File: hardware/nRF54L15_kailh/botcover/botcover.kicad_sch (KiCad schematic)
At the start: 143 parts

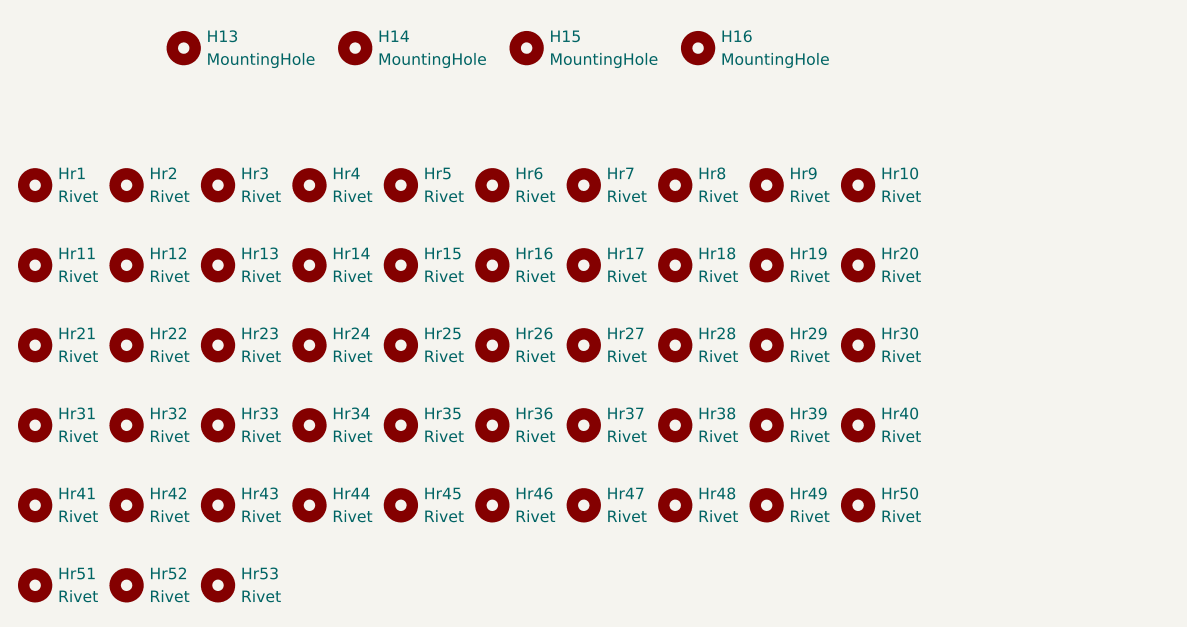
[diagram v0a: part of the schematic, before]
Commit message: M  hardware/nRF54L15_kailh/border.py M  hardware/nRF54L15_kailh/botcover/botcover.kicad_pcb M  hardware/nRF54L15_kailh/botcover/botcover.kicad_sch M  hardware/nRF54L15_kailh/pcb/pcb.kicad_pcb M  hardware/nRF54L15_kailh/pcb/pcb.kicad_sch M  hardware/nRF54L15_kailh/placefp.py A  hardware/nRF54L15_kailh/tmr-footprints/MountingHole_1.5mm_M1.4_NoPad.kicad_mod R  hardware/nRF54L15_kailh/tmr-footprints/SMTSO_M1.6.kicad_mod -> hardware/nRF54L15_kailh/tmr-footprints/SMTSO_M1.4_M1.6.kicad_mod
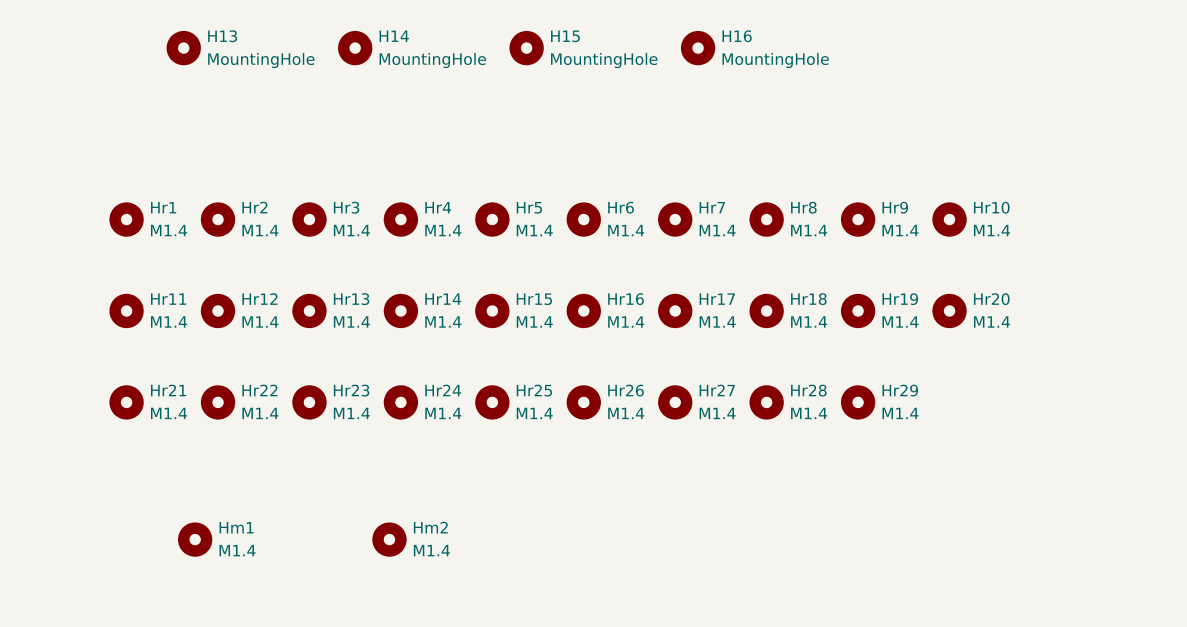
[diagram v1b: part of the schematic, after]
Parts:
- removed Hr30, Hr31, Hr32, Hr33, Hr34, Hr35, Hr36, Hr37, Hr38, Hr39, Hr40, Hr41, Hr42, Hr43, Hr44, Hr45, Hr46, Hr47, Hr48, Hr49, Hr50, Hr51, Hr52, Hr53: Rivet, tmr-lib:RivetClearanceHole_1.5mm, symbol Mechanical:MountingHole
- added Hm1, Hm2: M1.4, tmr-lib:MountingHole_1.5mm_M1.4_NoPad, symbol Mechanical:MountingHole
- Hr1, Hr10, Hr11, Hr12, Hr13, Hr14, Hr15, Hr16, Hr17, Hr18, Hr19, Hr2, Hr20, Hr21, Hr22, Hr23, Hr24, Hr25, Hr26, Hr27, Hr28, Hr29, Hr3, Hr4, Hr5, Hr6, Hr7, Hr8, Hr9: value Rivet -> M1.4; footprint tmr-lib:RivetClearanceHole_1.5mm -> tmr-lib:MountingHole_1.5mm_M1.4_NoPad
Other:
- moved on the sheet: Hr1

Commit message: M  .gitignore A  hardware/nRF54L15_gateron_kailh_TMR2615/LED.kicad_sch A  hardware/nRF54L15_gateron_kailh_TMR2615/fp-lib-table A  hardware/nRF54L15_gateron_kailh_TMR2615/nRF54L15_gateron_kailh_TMR2615.kicad_pcb A  hardware/nRF54L15_gateron_kailh_TMR2615/nRF54L15_gateron_kailh_TMR2615.kicad_prl A  hardware/nRF54L15_gateron_kailh_TMR2615/nRF54L15_gateron_kailh_TMR2615.kicad_pro A  hardware/nRF54L15_gateron_kailh_TMR2615/nRF54L15_gateron_kailh_TMR2615.kicad_sch A  hardware/nRF54L15_gateron_kailh_TMR2615/pcb-eagle-import.kicad_sym A  hardware/nRF54L15_gateron_kailh_TMR2615/switch.kicad_sch A  hardware/nRF54L15_gateron_kailh_TMR2615/sym-lib-table M  hardware/nRF54L15_kailh/border.py A  hardware/nRF54L15_kailh/botcase/botcase-Edge_Cuts.pdf M  hardware/nRF54L15_kailh/botcase/botcase.kicad_pcb M  hardware/nRF54L15_kailh/botcase/botcase.kicad_sch M  hardware/nRF54L15_kailh/botcover/botcover.kicad_pcb M  hardware/nRF54L15_kailh/botcover/botcover.kicad_sch M  hardware/nRF54L15_kailh/placefp.py A  hardware/nRF54L15_kailh/rebuild_board.py A  hardware/nRF54L15_kailh/run.sh M  hardware/nRF54L15_kailh/swplate/swplate.kicad_pcb M  hardware/nRF54L15_kailh/swplate/swplate.kicad_sch A  hardware/nRF54L15_kailh/tmr-footprints/Kailh_gateron_sw_lowpro.kicad_mod M  hardware/nRF54L15_kailh/tmr-footprints/Kailh_sw_lowpro.kicad_mod A  hardware/nRF54L15_kailh/tmr-footprints/M1.4_tap.kicad_mod A  hardware/nRF54L15_kailh/tmr-footprints/M2.5_tap.kicad_mod A  hardware/nRF54L15_kailh/tmr-footprints/MountingHole_1.6mm_M1.4_NoPad.kicad_mod M  hardware/nRF54L15_kailh/topcase/topcase.kicad_pcb A  hardware/nRF54L15_kailh/wristrest/fp-lib-table A  hardware/nRF54L15_kailh/wristrest/sym-lib-table A  hardware/nRF54L15_kailh/wristrest/wristrest.kicad_pcb A  hardware/nRF54L15_kailh/wristrest/wristrest.kicad_prl A  hardware/nRF54L15_kailh/wristrest/wristrest.kicad_pro A  hardware/nRF54L15_kailh/wristrest/wristrest.kicad_sch
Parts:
- Hm1, Hm2, Hr1, Hr10, Hr11, Hr12, Hr13, Hr14, Hr15, Hr16, Hr17, Hr18, Hr19, Hr2, Hr20, Hr21, Hr22, Hr23, Hr24, Hr25, Hr26, Hr27, Hr28, Hr29, Hr3, Hr4, Hr5, Hr6, Hr7, Hr8, Hr9: footprint tmr-lib:MountingHole_1.5mm_M1.4_NoPad -> tmr-lib:MountingHole_1.6mm_M1.4_NoPad
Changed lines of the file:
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@@
 			)
 		)
-		(property "Footprint" "tmr-lib:MountingHole_1.5mm_M1.4_NoPad"
+		(property "Footprint" "tmr-lib:MountingHole_1.6mm_M1.4_NoPad"
 			(at 40.64 137.16 0)
 			(effects
@@
 			)
 		)
-		(property "Footprint" "tmr-lib:MountingHole_1.5mm_M1.4_NoPad"
+		(property "Footprint" "tmr-lib:MountingHole_1.6mm_M1.4_NoPad"
 			(at 121.92 147.32 0)
 			(effects
@@
 			)
 		)
-		(property "Footprint" "tmr-lib:MountingHole_1.5mm_M1.4_NoPad"
+		(property "Footprint" "tmr-lib:MountingHole_1.6mm_M1.4_NoPad"
 			(at 60.96 147.32 0)
 			(effects
@@
 			)
 		)
-		(property "Footprint" "tmr-lib:MountingHole_1.5mm_M1.4_NoPad"
+		(property "Footprint" "tmr-lib:MountingHole_1.6mm_M1.4_NoPad"
 			(at 91.44 147.32 0)
 			(effects
@@
 			)
 		)
-		(property "Footprint" "tmr-lib:MountingHole_1.5mm_M1.4_NoPad"
+		(property "Footprint" "tmr-lib:MountingHole_1.6mm_M1.4_NoPad"
 			(at 60.96 137.16 0)
 			(effects
@@
 			)
 		)
-		(property "Footprint" "tmr-lib:MountingHole_1.5mm_M1.4_NoPad"
+		(property "Footprint" "tmr-lib:MountingHole_1.6mm_M1.4_NoPad"
 			(at 40.64 157.48 0)
 			(effects
@@
 			)
 		)
-		(property "Footprint" "tmr-lib:MountingHole_1.5mm_M1.4_NoPad"
+		(property "Footprint" "tmr-lib:MountingHole_1.6mm_M1.4_NoPad"
 			(at 30.48 137.16 0)
 			(effects
@@
 			)
 		)
-		(property "Footprint" "tmr-lib:MountingHole_1.5mm_M1.4_NoPad"
+		(property "Footprint" "tmr-lib:MountingHole_1.6mm_M1.4_NoPad"
 			(at 81.28 137.16 0)
 			(effects
@@
 			)
 		)
-		(property "Footprint" "tmr-lib:MountingHole_1.5mm_M1.4_NoPad"
+		(property "Footprint" "tmr-lib:MountingHole_1.6mm_M1.4_NoPad"
 			(at 71.12 157.48 0)
 			(effects
@@
 			)
 		)
-		(property "Footprint" "tmr-lib:MountingHole_1.5mm_M1.4_NoPad"
+		(property "Footprint" "tmr-lib:MountingHole_1.6mm_M1.4_NoPad"
 			(at 71.12 137.16 0)
 			(effects
@@
 			)
 		)
-		(property "Footprint" "tmr-lib:MountingHole_1.5mm_M1.4_NoPad"
+		(property "Footprint" "tmr-lib:MountingHole_1.6mm_M1.4_NoPad"
 			(at 111.76 137.16 0)
 			(effects
@@
 			)
 		)
-		(property "Footprint" "tmr-lib:MountingHole_1.5mm_M1.4_NoPad"
+		(property "Footprint" "tmr-lib:MountingHole_1.6mm_M1.4_NoPad"
 			(at 121.92 137.16 0)
 			(effects
@@
 			)
 		)
-		(property "Footprint" "tmr-lib:MountingHole_1.5mm_M1.4_NoPad"
+		(property "Footprint" "tmr-lib:MountingHole_1.6mm_M1.4_NoPad"
 			(at 101.6 147.32 0)
 			(effects
@@
 			)
 		)
-		(property "Footprint" "tmr-lib:MountingHole_1.5mm_M1.4_NoPad"
+		(property "Footprint" "tmr-lib:MountingHole_1.6mm_M1.4_NoPad"
 			(at 30.48 147.32 0)
 			(effects
@@
 			)
 		)
-		(property "Footprint" "tmr-lib:MountingHole_1.5mm_M1.4_NoPad"
+		(property "Footprint" "tmr-lib:MountingHole_1.6mm_M1.4_NoPad"
 			(at 38.1 172.72 0)
 			(effects
@@
 			)
 		)
-		(property "Footprint" "tmr-lib:MountingHole_1.5mm_M1.4_NoPad"
+		(property "Footprint" "tmr-lib:MountingHole_1.6mm_M1.4_NoPad"
 			(at 30.48 157.48 0)
 			(effects
@@
 			)
 		)
-		(property "Footprint" "tmr-lib:MountingHole_1.5mm_M1.4_NoPad"
+		(property "Footprint" "tmr-lib:MountingHole_1.6mm_M1.4_NoPad"
 			(at 101.6 137.16 0)
 			(effects
@@
 			)
 		)
-		(property "Footprint" "tmr-lib:MountingHole_1.5mm_M1.4_NoPad"
+		(property "Footprint" "tmr-lib:MountingHole_1.6mm_M1.4_NoPad"
 			(at 71.12 147.32 0)
 			(effects
@@
 			)
 		)
-		(property "Footprint" "tmr-lib:MountingHole_1.5mm_M1.4_NoPad"
+		(property "Footprint" "tmr-lib:MountingHole_1.6mm_M1.4_NoPad"
 			(at 81.28 147.32 0)
 			(effects
@@
 			)
 		)
-		(property "Footprint" "tmr-lib:MountingHole_1.5mm_M1.4_NoPad"
+		(property "Footprint" "tmr-lib:MountingHole_1.6mm_M1.4_NoPad"
 			(at 101.6 157.48 0)
 			(effects
@@
 			)
 		)
-		(property "Footprint" "tmr-lib:MountingHole_1.5mm_M1.4_NoPad"
+		(property "Footprint" "tmr-lib:MountingHole_1.6mm_M1.4_NoPad"
 			(at 91.44 137.16 0)
 			(effects
@@
 			)
 		)
-		(property "Footprint" "tmr-lib:MountingHole_1.5mm_M1.4_NoPad"
+		(property "Footprint" "tmr-lib:MountingHole_1.6mm_M1.4_NoPad"
 			(at 81.28 157.48 0)
 			(effects
@@
 			)
 		)
-		(property "Footprint" "tmr-lib:MountingHole_1.5mm_M1.4_NoPad"
+		(property "Footprint" "tmr-lib:MountingHole_1.6mm_M1.4_NoPad"
 			(at 50.8 137.16 0)
 			(effects
@@
 			)
 		)
-		(property "Footprint" "tmr-lib:MountingHole_1.5mm_M1.4_NoPad"
+		(property "Footprint" "tmr-lib:MountingHole_1.6mm_M1.4_NoPad"
 			(at 50.8 157.48 0)
 			(effects
@@
 			)
 		)
-		(property "Footprint" "tmr-lib:MountingHole_1.5mm_M1.4_NoPad"
+		(property "Footprint" "tmr-lib:MountingHole_1.6mm_M1.4_NoPad"
 			(at 40.64 147.32 0)
 			(effects
@@
 			)
 		)
-		(property "Footprint" "tmr-lib:MountingHole_1.5mm_M1.4_NoPad"
+		(property "Footprint" "tmr-lib:MountingHole_1.6mm_M1.4_NoPad"
 			(at 111.76 157.48 0)
 			(effects
@@
 			)
 		)
-		(property "Footprint" "tmr-lib:MountingHole_1.5mm_M1.4_NoPad"
+		(property "Footprint" "tmr-lib:MountingHole_1.6mm_M1.4_NoPad"
 			(at 91.44 157.48 0)
 			(effects
@@
 			)
 		)
-		(property "Footprint" "tmr-lib:MountingHole_1.5mm_M1.4_NoPad"
+		(property "Footprint" "tmr-lib:MountingHole_1.6mm_M1.4_NoPad"
 			(at 111.76 147.32 0)
 			(effects
@@
 			)
 		)
-		(property "Footprint" "tmr-lib:MountingHole_1.5mm_M1.4_NoPad"
+		(property "Footprint" "tmr-lib:MountingHole_1.6mm_M1.4_NoPad"
 			(at 60.96 157.48 0)
 			(effects
@@
 			)
 		)
-		(property "Footprint" "tmr-lib:MountingHole_1.5mm_M1.4_NoPad"
+		(property "Footprint" "tmr-lib:MountingHole_1.6mm_M1.4_NoPad"
 			(at 59.69 172.72 0)
 			(effects
@@
 			)
 		)
-		(property "Footprint" "tmr-lib:MountingHole_1.5mm_M1.4_NoPad"
+		(property "Footprint" "tmr-lib:MountingHole_1.6mm_M1.4_NoPad"
 			(at 50.8 147.32 0)
 			(effects

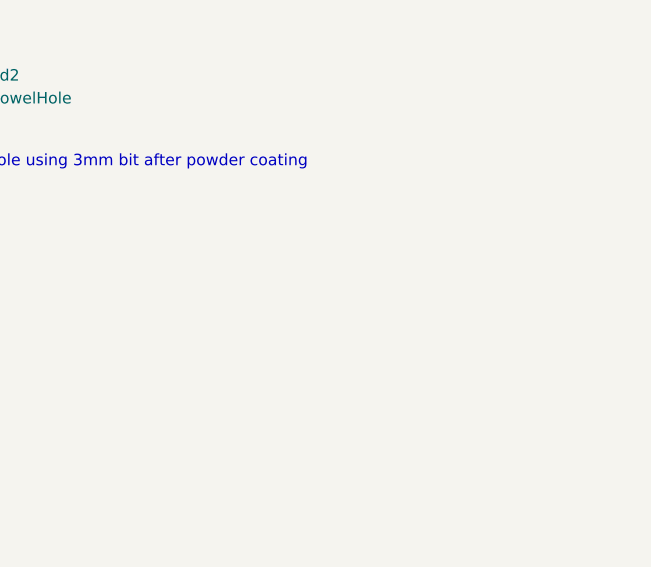
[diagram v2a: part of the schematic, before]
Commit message: M  hardware/nRF54L15_kailh/border.py M  hardware/nRF54L15_kailh/botcover/botcover.kicad_pcb M  hardware/nRF54L15_kailh/botcover/botcover.kicad_sch M  hardware/nRF54L15_kailh/placefp.py A  hardware/nRF54L15_kailh/tmr-footprints/Aliexpress_SW_TACT_4x4x1.5mm_hole_only.kicad_mod
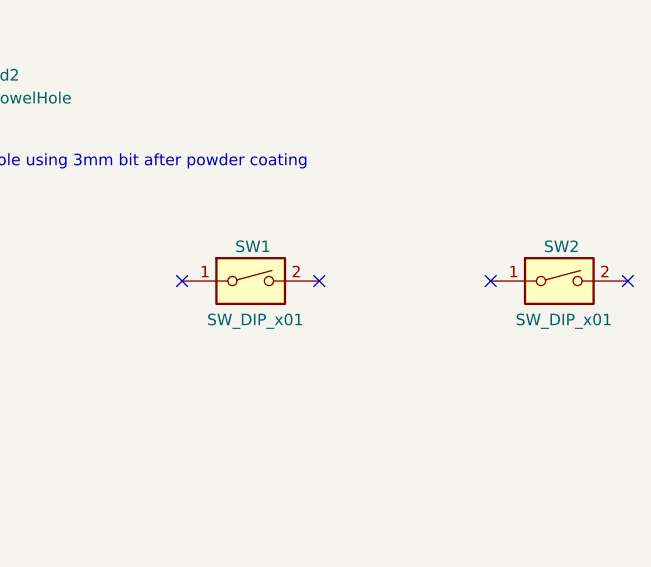
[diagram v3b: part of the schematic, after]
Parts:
- added SW1, SW2: SW_DIP_x01, tmr-lib:Aliexpress_SW_TACT_4x4x1.5mm_hole_only, symbol Switch:SW_DIP_x01
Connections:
- no-connect marks 0 -> 4
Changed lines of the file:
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@@
 		)
 	)
+	(no_connect
+		(at 195.58 115.57)
+	)
+	(no_connect
+		(at 229.87 115.57)
+	)
+	(no_connect
+		(at 214.63 115.57)
+	)
+	(no_connect
+		(at 180.34 115.57)
+	)
 	(symbol
 		(lib_id "tmr-lib:SWHole")
@@
 	)
 	(symbol
+		(lib_id "Switch:SW_DIP_x01")
+		(at 222.25 115.57 0)
+		(unit 1)
+		(exclude_from_sim no)
+		(in_bom yes)
+		(on_board yes)
+		(dnp no)
+		(property "Reference" "SW2"
+			(at 222.504 111.76 0)
+			(effects
+				(font
+					(size 1.27 1.27)
+				)
+			)
+		)
+		(property "Value" "SW_DIP_x01"
+			(at 222.758 119.888 0)
+			(effects
+				(font
+					(size 1.27 1.27)
+				)
+			)
+		)
+		(property "Footprint" "tmr-lib:Aliexpress_SW_TACT_4x4x1.5mm_hole_only"
+			(at 222.25 115.57 0)
+			(effects
+				(font
+					(size 1.27 1.27)
+				)
+				(hide yes)
+			)
+		)
+		(property "Datasheet" "~"
+			(at 222.25 115.57 0)
+			(effects
+				(font
+					(size 1.27 1.27)
+				)
+				(hide yes)
+			)
+		)
+		(property "Description" "1x DIP Switch, Single Pole Single Throw (SPST) switch, small symbol"
+			(at 222.25 115.57 0)
+			(effects
+				(font
+					(size 1.27 1.27)
+				)
+				(hide yes)
+			)
+		)
+		(pin "1"
+		)
+		(pin "2"
+		)
+		(instances
+			(project "botcover"
+				(path "/4c67809e-1748-4898-89f6-ff92314048f2"
+					(reference "SW2")
+					(unit 1)
+				)
+			)
+		)
+	)
+	(symbol
 		(lib_id "Mechanical:MountingHole")
 		(at 71.12 157.48 0)
@@
 					(unit 1)
 				)
+			)
+		)
+	)
+	(symbol
+		(lib_id "Switch:SW_DIP_x01")
+		(at 187.96 115.57 0)
+		(unit 1)
+		(exclude_from_sim no)
+		(in_bom yes)
+		(on_board yes)
+		(dnp no)
+		(property "Reference" "SW1"
+			(at 188.214 111.76 0)
+			(effects
+				(font
+					(size 1.27 1.27)
+				)
+			)
+		)
+		(property "Value" "SW_DIP_x01"
+			(at 188.468 119.888 0)
+			(effects
+				(font
+					(size 1.27 1.27)
+				)
+			)
+		)
+		(property "Footprint" "tmr-lib:Aliexpress_SW_TACT_4x4x1.5mm_hole_only"
+			(at 187.96 115.57 0)
+			(effects
+				(font
+					(size 1.27 1.27)
+				)
+				(hide yes)
+			)
+		)
+		(property "Datasheet" "~"
+			(at 187.96 115.57 0)
+			(effects
+				(font
+					(size 1.27 1.27)
+				)
+				(hide yes)
+			)
+		)
+		(property "Description" "1x DIP Switch, Single Pole Single Throw (SPST) switch, small symbol"
+			(at 187.96 115.57 0)
+			(effects
+				(font
+					(size 1.27 1.27)
+				)
+				(hide yes)
+			)
+		)
+		(pin "1"
+		)
+		(pin "2"
+		)
+		(instances
+			(project "botcover"
+				(path "/4c67809e-1748-4898-89f6-ff92314048f2"
+					(reference "SW1")
+					(unit 1)
+				)
